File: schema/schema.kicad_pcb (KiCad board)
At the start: 2 copper layers, 88.9 x 55.9 mm, 13 parts, among them J1 Conn_01x04_Male, J2 Conn_01x04_Male, J3 Conn_01x05_Male

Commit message: Update PCB
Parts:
- added REF**: MountingHole_2.2mm_M2_Pad, MountingHole:MountingHole_2.2mm_M2_Pad, F.Cu at (176.5, 114.3)
- C2, C4: footprint Capacitors_THT:CP_Radial_D5.0mm_P2.50mm -> Capacitor_THT:CP_Radial_D8.0mm_P5.00mm
- moved REF** 6.35 mm to (94.0, 114.3)
- moved REF** 6.35 mm to (95.2, 66.0)
- moved REF** 5.24 mm to (170.2, 66.0)
- moved C2 1.19 mm to (143.4, 95.2)
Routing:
- net +12V: track 55.6 -> 56.9 mm
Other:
- board text added: ": 7 : 8 : 9 : 10 : 11 : 12 : 13"
- board text added: ": A9 : A10 : A11 : A12 : A13 : A14 : A15"
- board text added: "Ascension Droite En MS1 MS2 MS3 RST STEP DIR"
- board text added: "Déclinaison En MS1 MS2 MS3 RST STEP DIR"
- board text removed: "Ascension Droite En : A9 MS1 : A10 MS2 : A11 MS3 : A12 RST : A13 STEP : A14 DIR : A15"
- board text removed: "Déclinaison En : 7 MS1 : 8 MS2 : 9 MS3 : 10 RST : 11 STEP : 12 DIR : 13"

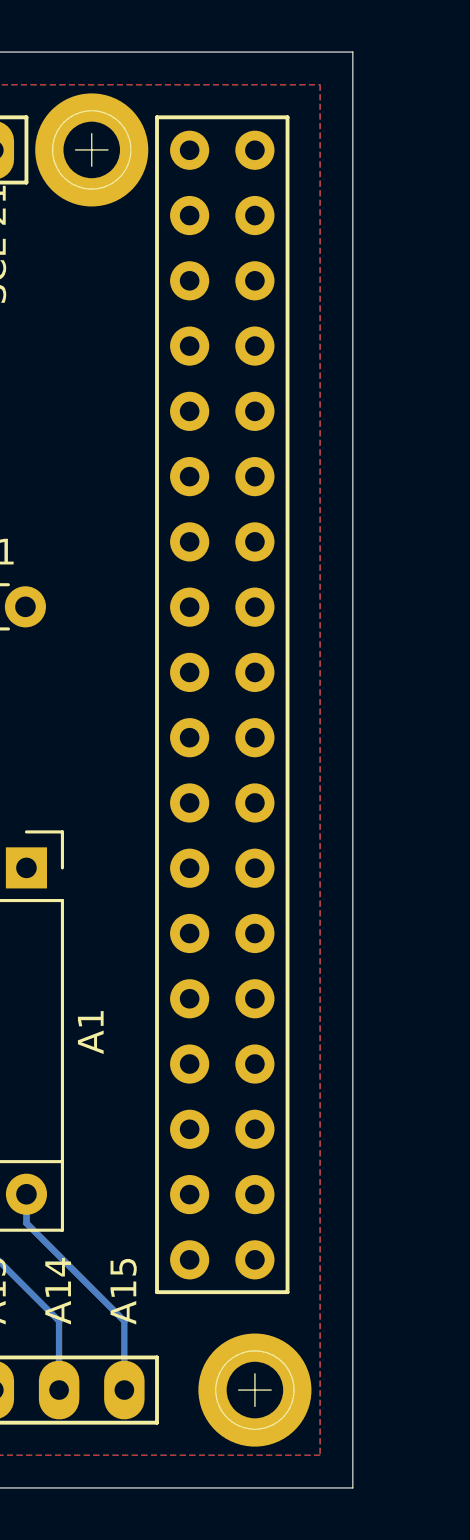
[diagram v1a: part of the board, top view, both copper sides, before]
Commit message: Deplacement des trous
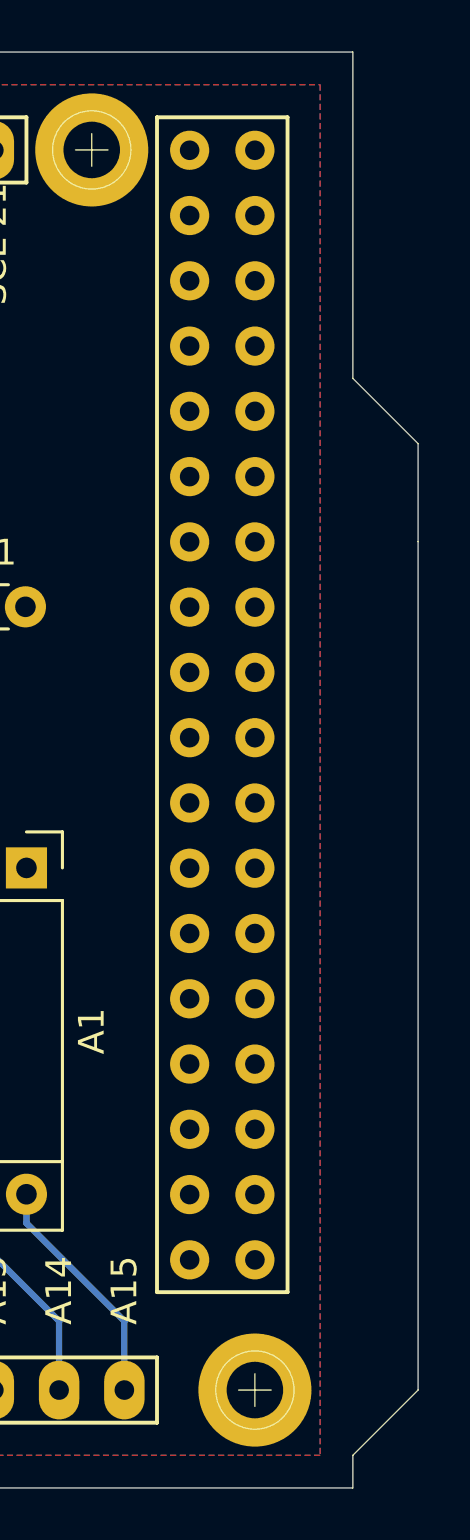
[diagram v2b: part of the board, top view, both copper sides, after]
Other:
- board size 88.9 x 55.9 mm -> 91.4 x 55.9 mm
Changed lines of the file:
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@@
   (general
     (thickness 1.6)
-    (drawings 82)
+    (drawings 87)
     (tracks 129)
     (zones 0)
@@
     )
   )
+  (gr_line (start 182.88 77.47) (end 182.88 81.28) (layer Edge.Cuts) (width 0.05))
+  (gr_line (start 180.34 74.93) (end 182.88 77.47) (layer Edge.Cuts) (width 0.05))
+  (gr_line (start 180.34 62.23) (end 180.34 74.93) (layer Edge.Cuts) (width 0.05))
+  (gr_line (start 182.88 114.3) (end 182.88 81.28) (layer Edge.Cuts) (width 0.05))
+  (gr_line (start 180.34 116.84) (end 182.88 114.3) (layer Edge.Cuts) (width 0.05))
+  (gr_line (start 180.34 118.11) (end 180.34 116.84) (layer Edge.Cuts) (width 0.05))
   (gr_text "\n: 7\n: 8\n: 9\n: 10\n: 11  \n: 12\n: 13" (at 106.68 82.55) (layer B.SilkS)
     (effects (font (size 0.7 0.7) (thickness 0.15)) (justify left mirror))
@@
   (gr_line (start 91.44 118.11) (end 91.44 62.23) (layer Edge.Cuts) (width 0.05))
   (gr_line (start 180.34 118.11) (end 91.44 118.11) (layer Edge.Cuts) (width 0.05))
-  (gr_line (start 180.34 62.23) (end 180.34 118.11) (layer Edge.Cuts) (width 0.05))
   (gr_line (start 91.44 62.23) (end 180.34 62.23) (layer Edge.Cuts) (width 0.05))
   (segment (start 115.57 73.66) (end 115.57 72.5347) (width 0.25) (layer B.Cu) (net 7))
